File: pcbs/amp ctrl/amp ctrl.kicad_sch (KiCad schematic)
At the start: 60 parts, among them J1 Conn_02x25_Odd_Even, J13 Conn_02x02, J4 Conn_01x02, U10 ADA4004-1, U70 MCP1754ST-3302

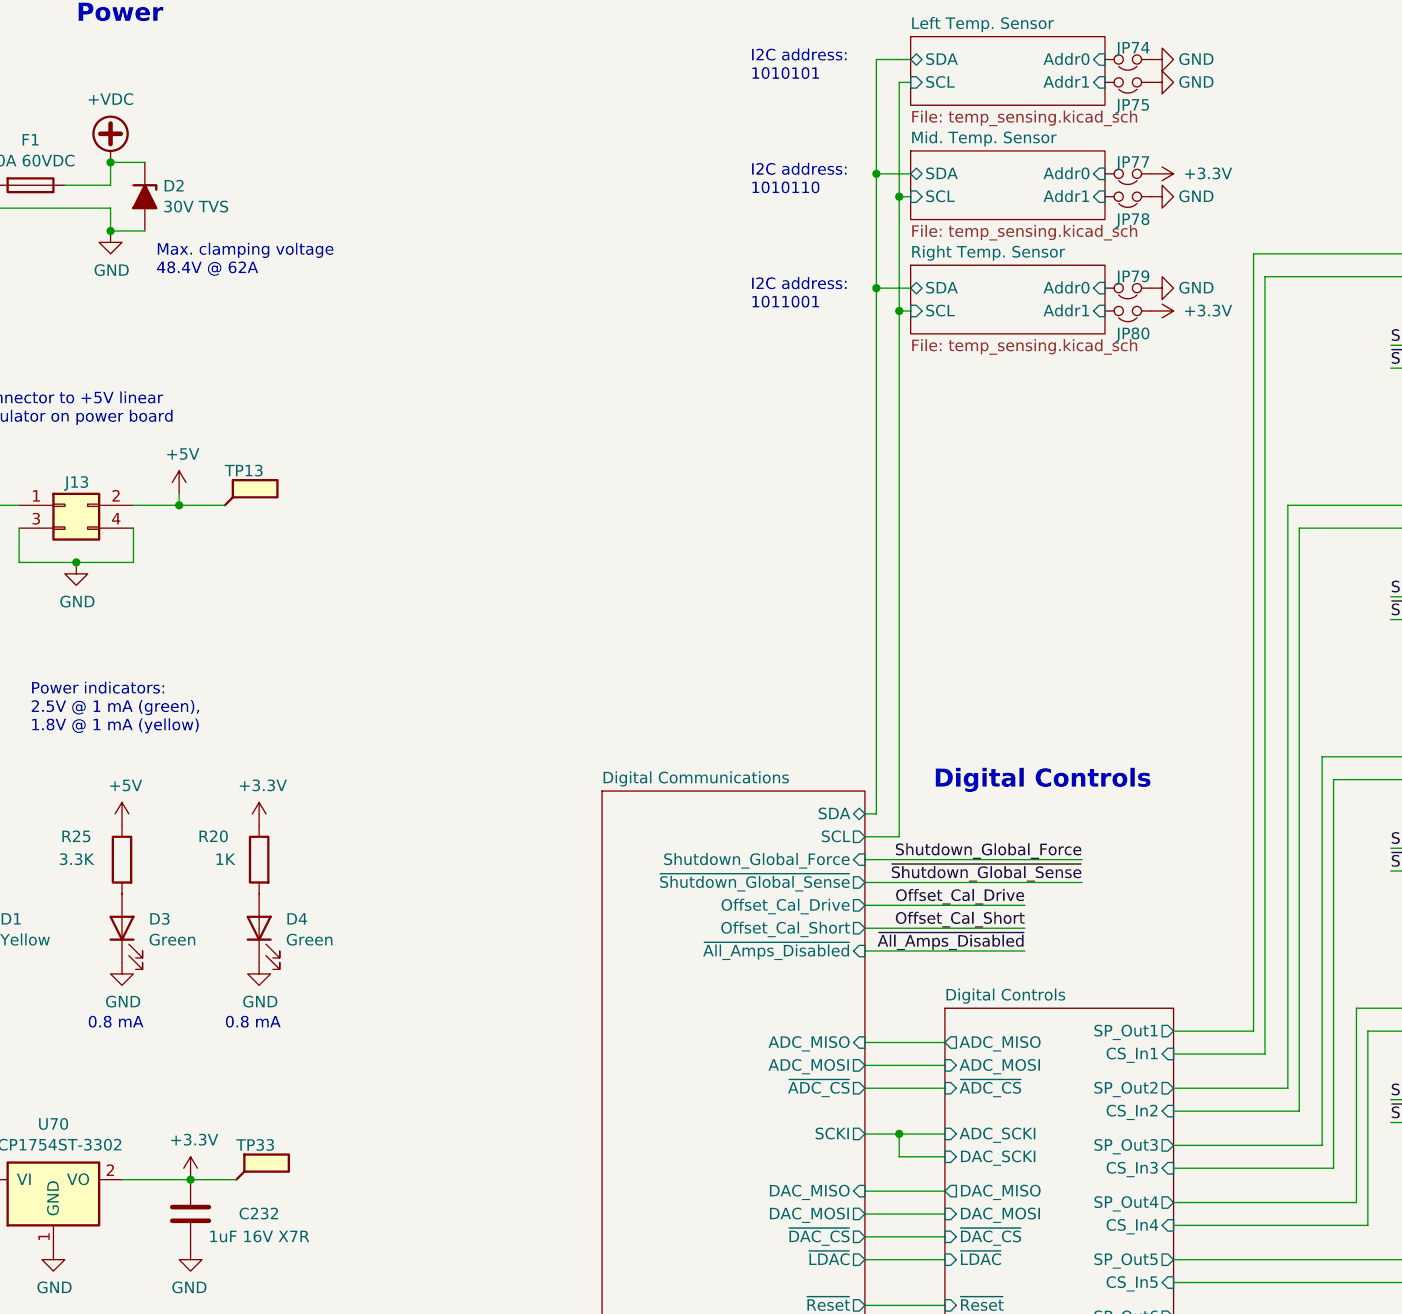
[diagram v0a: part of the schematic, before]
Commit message: Amp ctrl: lengthened ADC & DAC reset delay to ~50 ms (#14) Backplane: added clock multiplier for 10 Mhz scanner clock (fixes #21) Backplane: reduced R5 from 10 to 1 ohm, to avoid excessive voltage drop (#20) Backplane: replaced 15V regulator with efficient voltage limiter (#20) Backplane: changed all mounting holes to signal ground Backplane: replaced +2.5V regulator with a higher-current model to support FPGA I/O bank current draw Updated to KiCAD 8
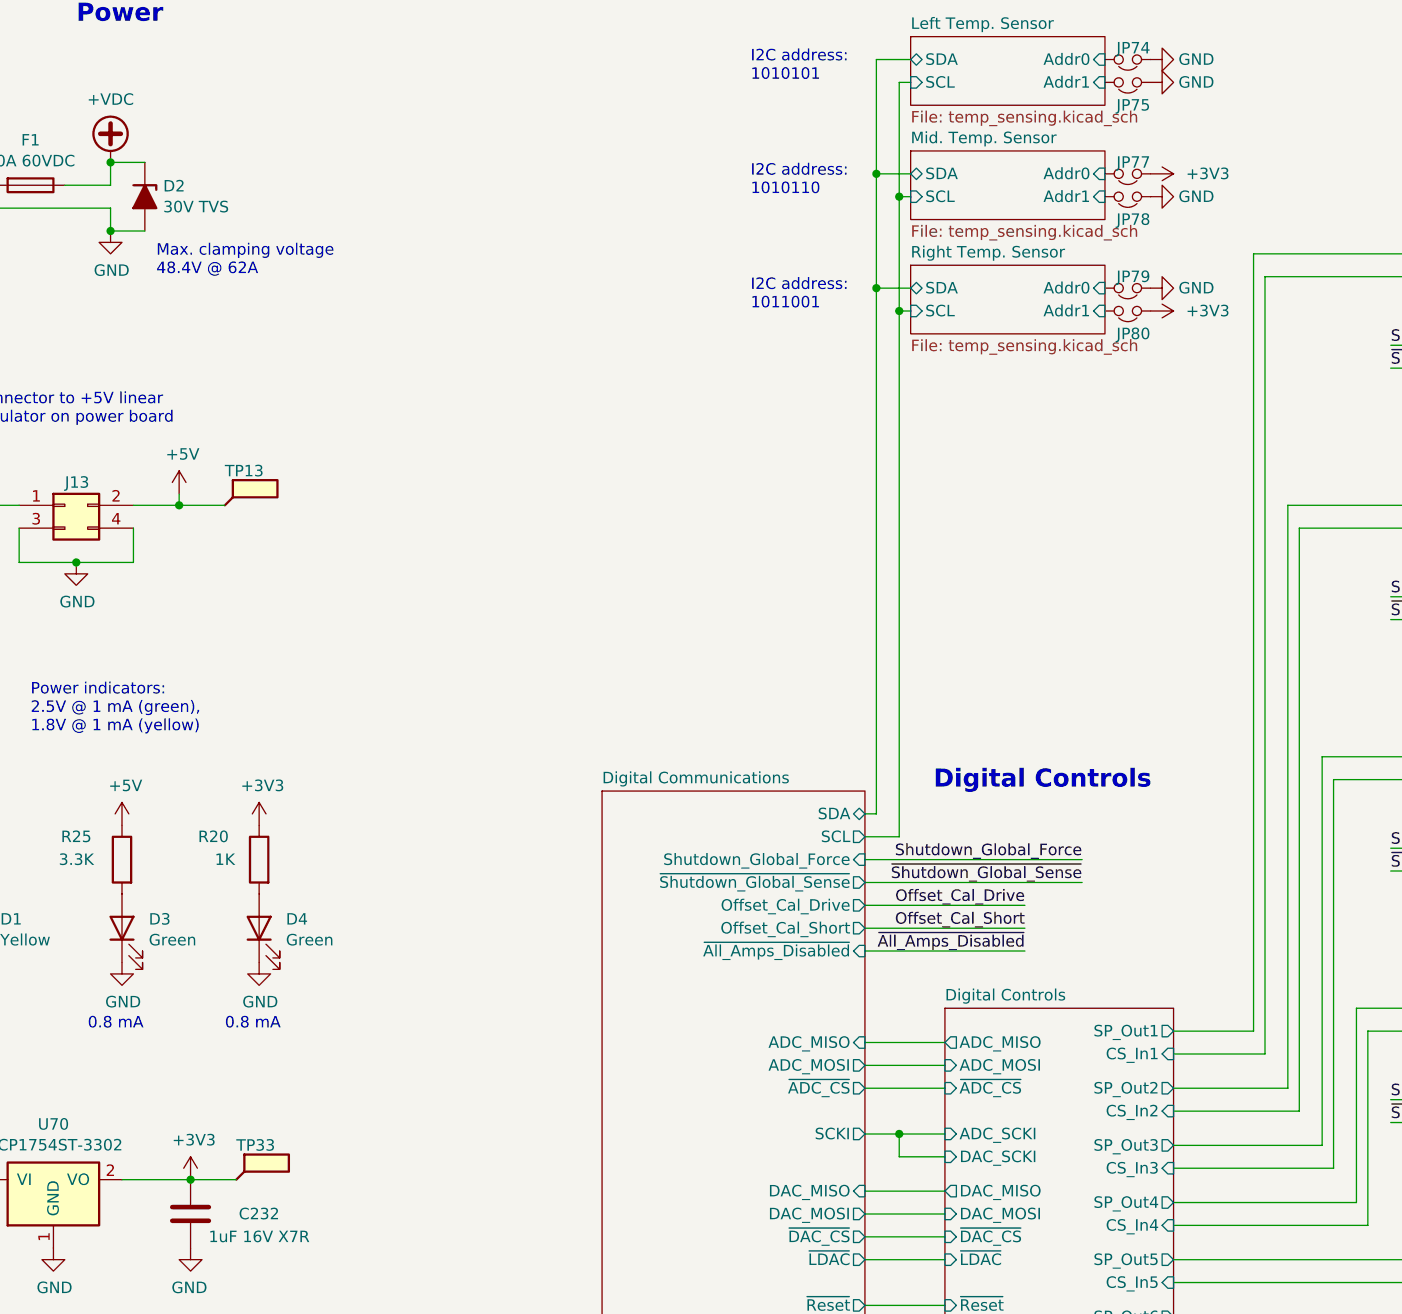
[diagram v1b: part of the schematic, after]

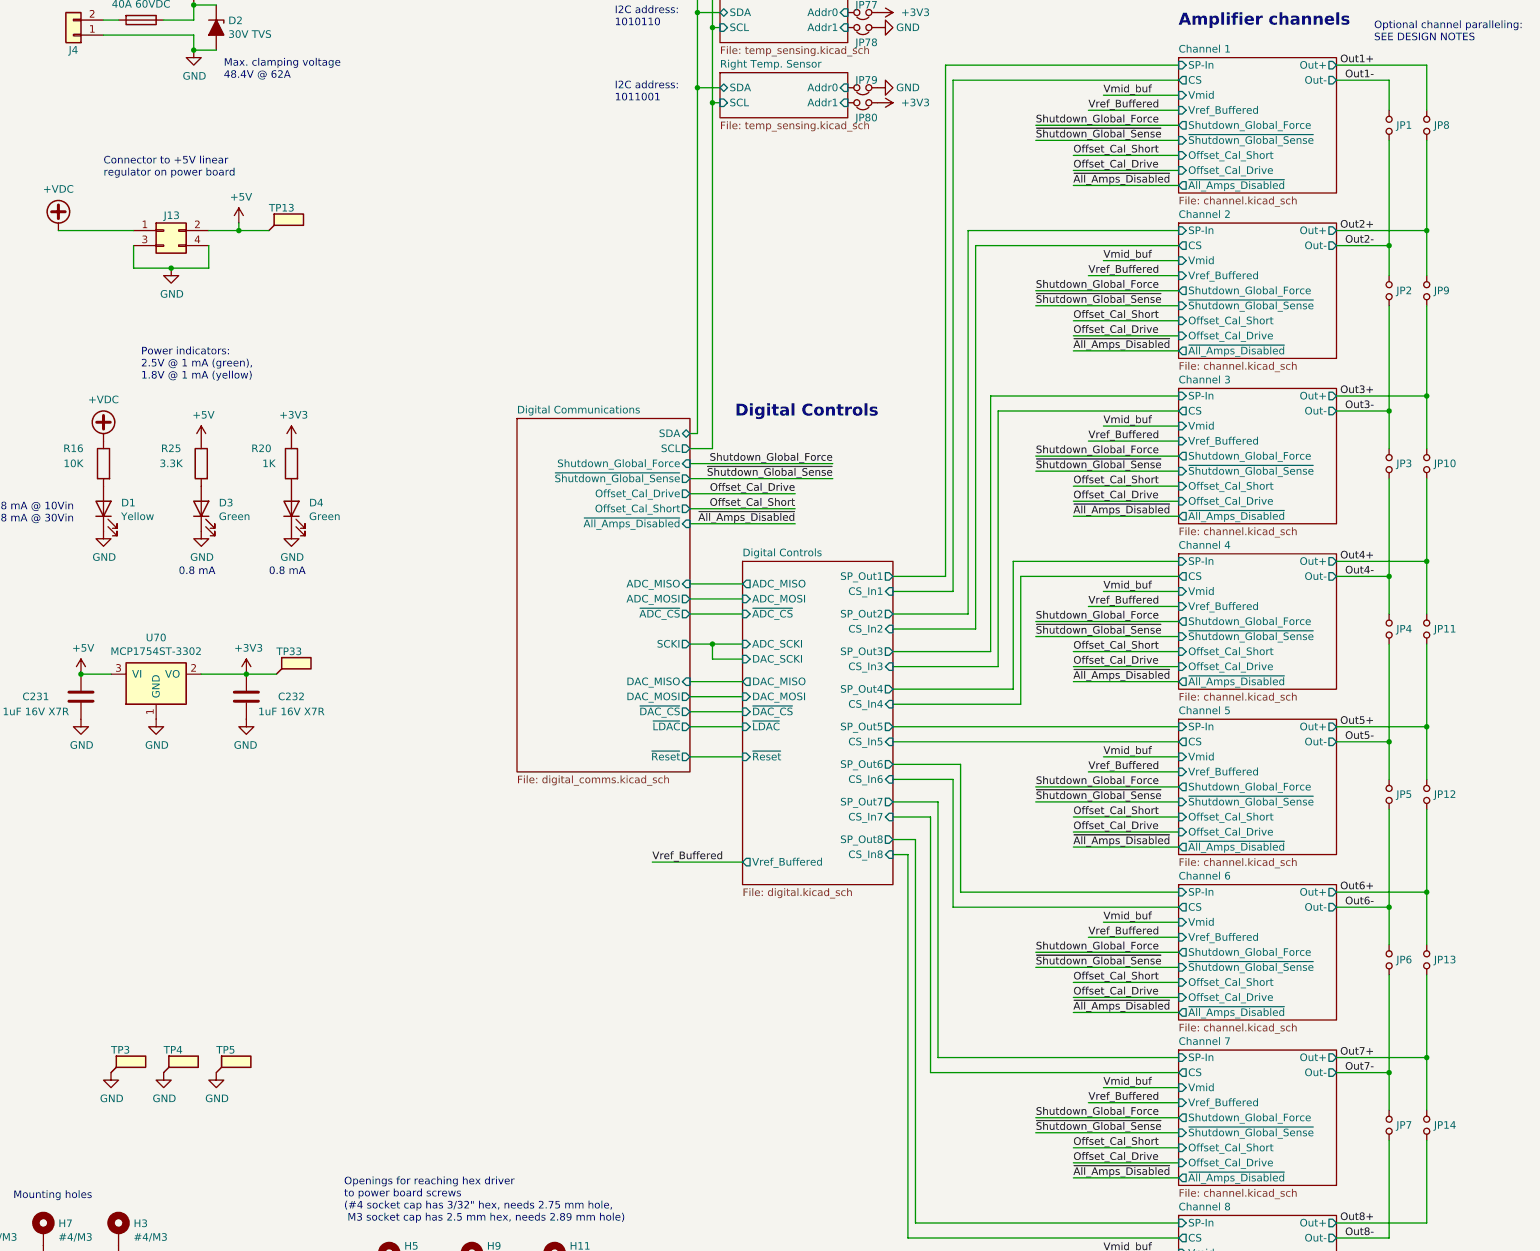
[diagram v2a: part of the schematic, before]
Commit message: Misc. cleanup for mfg & improvements
Minor backplane pinout doc corrections (SCKO5 polarity, clarified some descriptions)
Backplane: Added differential- and common-mode (to standoffs) power filtering, for EMI escaping over power wiring
Amp ctrl: Changed DAC testpoints from individual pads to Keystone 5019 for easier probing
Corrected part numbers, DNP vs. non-BOM-item indications, other misc. BOM issues
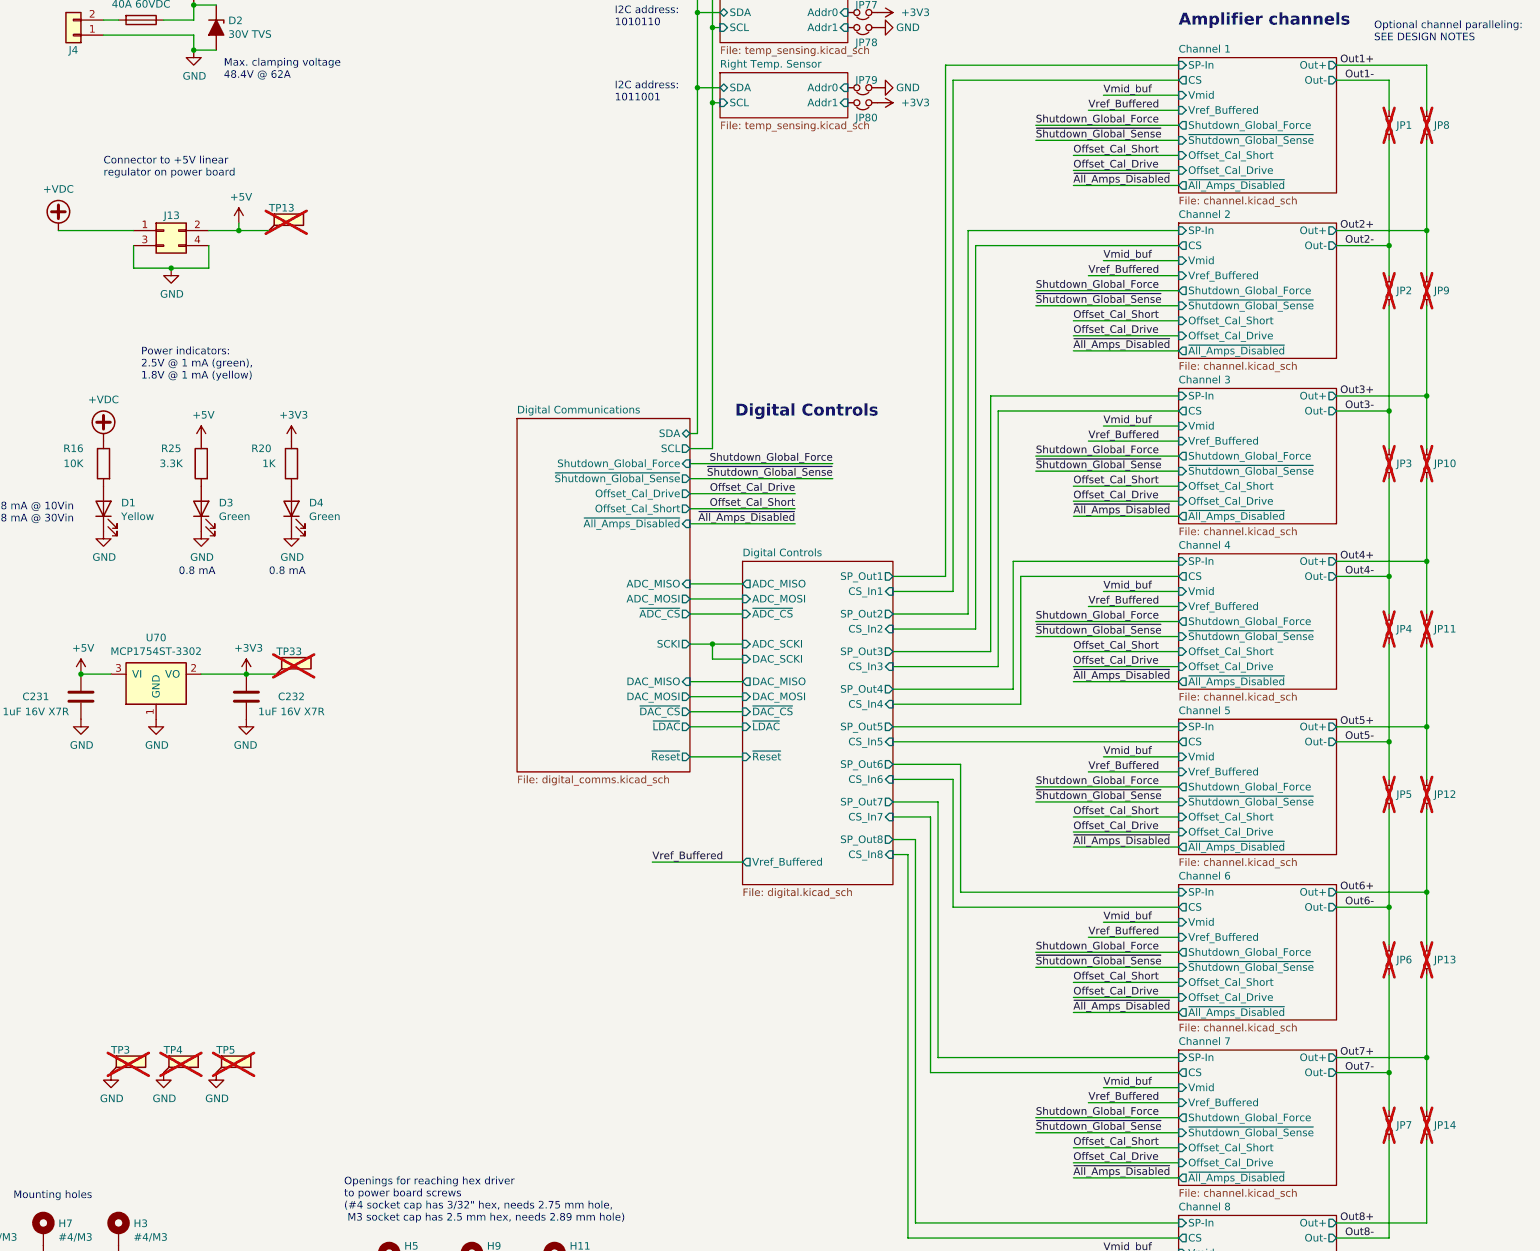
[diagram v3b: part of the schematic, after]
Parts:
- JP1, JP10, JP11, JP12, JP13, JP14, JP2, JP3, JP4, JP5, JP6, JP7, JP8, JP9: now not fitted
- TP13, TP3, TP33, TP4, TP5: footprint TestPoint:TestPoint_Keystone_5019_Minature -> Don_std:TestPoint_Keystone_5019_Minature; now not fitted
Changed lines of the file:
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@@
 		(in_bom yes)
 		(on_board yes)
-		(dnp no)
+		(dnp yes)
 		(property "Reference" "TP13"
 			(at 67.31 71.12 0)
@@
 			)
 		)
-		(property "Footprint" "TestPoint:TestPoint_Keystone_5019_Minature"
+		(property "Footprint" "Don_std:TestPoint_Keystone_5019_Minature"
 			(at 72.39 74.93 0)
 			(effects
@@
 		(in_bom yes)
 		(on_board yes)
-		(dnp no)
+		(dnp yes)
 		(property "Reference" "TP3"
 			(at 40.64 213.36 0)
@@
 			)
 		)
-		(property "Footprint" "TestPoint:TestPoint_Keystone_5019_Minature"
+		(property "Footprint" "Don_std:TestPoint_Keystone_5019_Minature"
 			(at 45.72 217.17 0)
 			(effects
@@
 		(in_bom yes)
 		(on_board yes)
-		(dnp no)
+		(dnp yes)
 		(property "Reference" "TP4"
 			(at 49.53 213.36 0)
@@
 			)
 		)
-		(property "Footprint" "TestPoint:TestPoint_Keystone_5019_Minature"
+		(property "Footprint" "Don_std:TestPoint_Keystone_5019_Minature"
 			(at 54.61 217.17 0)
 			(effects
@@
 		(in_bom yes)
 		(on_board yes)
-		(dnp no)
+		(dnp yes)
 		(property "Reference" "TP5"
 			(at 58.42 213.36 0)
@@
 			)
 		)
-		(property "Footprint" "TestPoint:TestPoint_Keystone_5019_Minature"
+		(property "Footprint" "Don_std:TestPoint_Keystone_5019_Minature"
 			(at 63.5 217.17 0)
 			(effects
@@
 		(in_bom yes)
 		(on_board yes)
-		(dnp no)
+		(dnp yes)
 		(property "Reference" "JP1"
 			(at 257.7592 57.15 90)
@@
 		(in_bom yes)
 		(on_board yes)
-		(dnp no)
+		(dnp yes)
 		(property "Reference" "JP8"
 			(at 264.1092 57.15 90)
@@
 		(in_bom yes)
 		(on_board yes)
-		(dnp no)
+		(dnp yes)
 		(property "Reference" "JP2"
 			(at 257.7592 85.09 90)
@@
 		(in_bom yes)
 		(on_board yes)
-		(dnp no)
+		(dnp yes)
 		(property "Reference" "JP9"
 			(at 264.1092 85.09 90)
@@
 		(in_bom yes)
 		(on_board yes)
-		(dnp no)
+		(dnp yes)
 		(property "Reference" "JP3"
 			(at 257.7592 114.3 90)
@@
 		(in_bom yes)
 		(on_board yes)
-		(dnp no)
+		(dnp yes)
 		(property "Reference" "JP10"
 			(at 264.1092 114.3 90)
@@
 		(in_bom yes)
 		(on_board yes)
-		(dnp no)
+		(dnp yes)
 		(property "Reference" "JP4"
 			(at 257.7592 142.24 90)
@@
 		(in_bom yes)
 		(on_board yes)
-		(dnp no)
+		(dnp yes)
 		(property "Reference" "JP11"
 			(at 264.1092 142.24 90)
@@
 		(in_bom yes)
 		(on_board yes)
-		(dnp no)
+		(dnp yes)
 		(property "Reference" "JP5"
 			(at 257.7592 170.18 90)
@@
 		(in_bom yes)
 		(on_board yes)
-		(dnp no)
+		(dnp yes)
 		(property "Reference" "JP12"
 			(at 264.1092 170.18 90)
@@
 		(in_bom yes)
 		(on_board yes)
-		(dnp no)
+		(dnp yes)
 		(property "Reference" "JP6"
 			(at 257.7592 198.12 90)
@@
 		(in_bom yes)
 		(on_board yes)
-		(dnp no)
+		(dnp yes)
 		(property "Reference" "JP13"
 			(at 264.1092 198.12 90)
@@
 		(in_bom yes)
 		(on_board yes)
-		(dnp no)
+		(dnp yes)
 		(property "Reference" "JP7"
 			(at 257.7592 226.06 90)
@@
 		(in_bom yes)
 		(on_board yes)
-		(dnp no)
+		(dnp yes)
 		(property "Reference" "JP14"
 			(at 264.1092 226.06 90)
@@
 		(in_bom yes)
 		(on_board yes)
-		(dnp no)
+		(dnp yes)
 		(property "Reference" "TP33"
 			(at 68.58 146.05 0)
@@
 			)
 		)
-		(property "Footprint" "TestPoint:TestPoint_Keystone_5019_Minature"
+		(property "Footprint" "Don_std:TestPoint_Keystone_5019_Minature"
 			(at 73.66 149.86 0)
 			(effects
